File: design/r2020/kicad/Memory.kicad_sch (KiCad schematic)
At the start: 10 parts, among them U1 SST39SF040, U2 SST39SF040, U3 AS6C4008-55PCN, U4 AS6C4008-55PCN

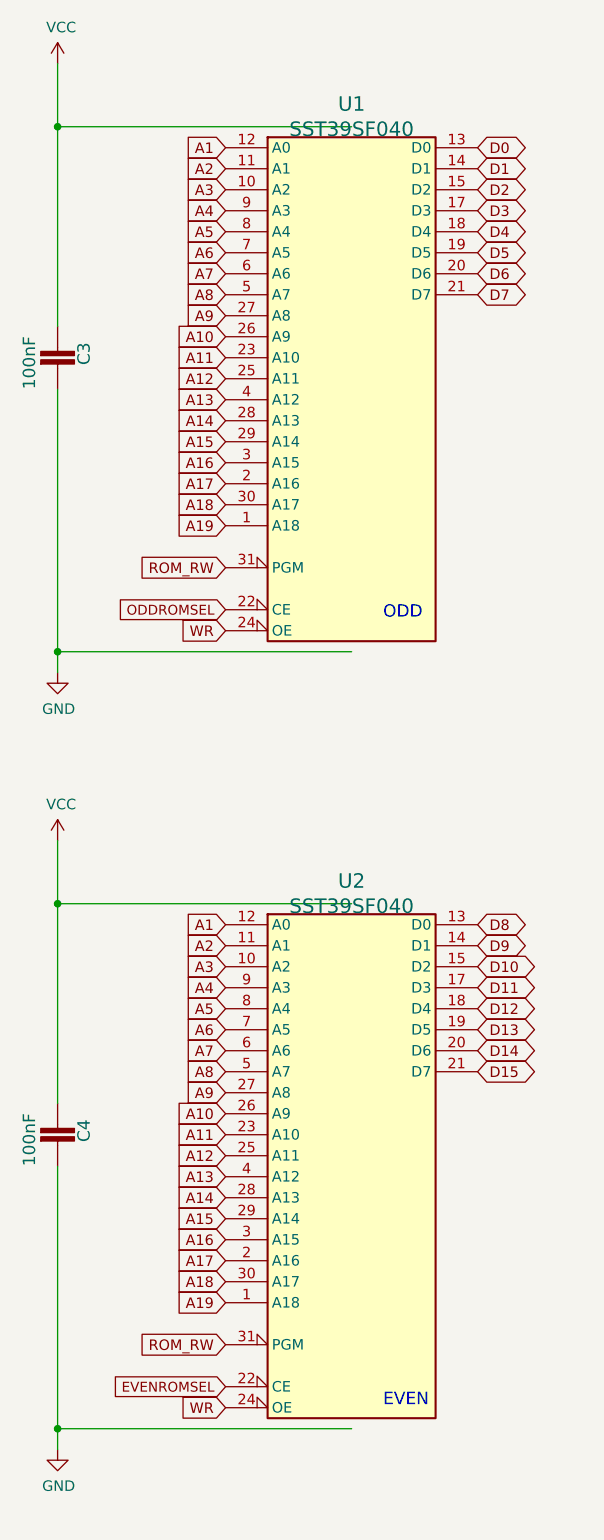
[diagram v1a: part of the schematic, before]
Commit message: Feature/kicad 7 (#388)
* Update r2 to Kicad 7
* Update r2020 to Kicad 7
* Complete Kicad 7 migration
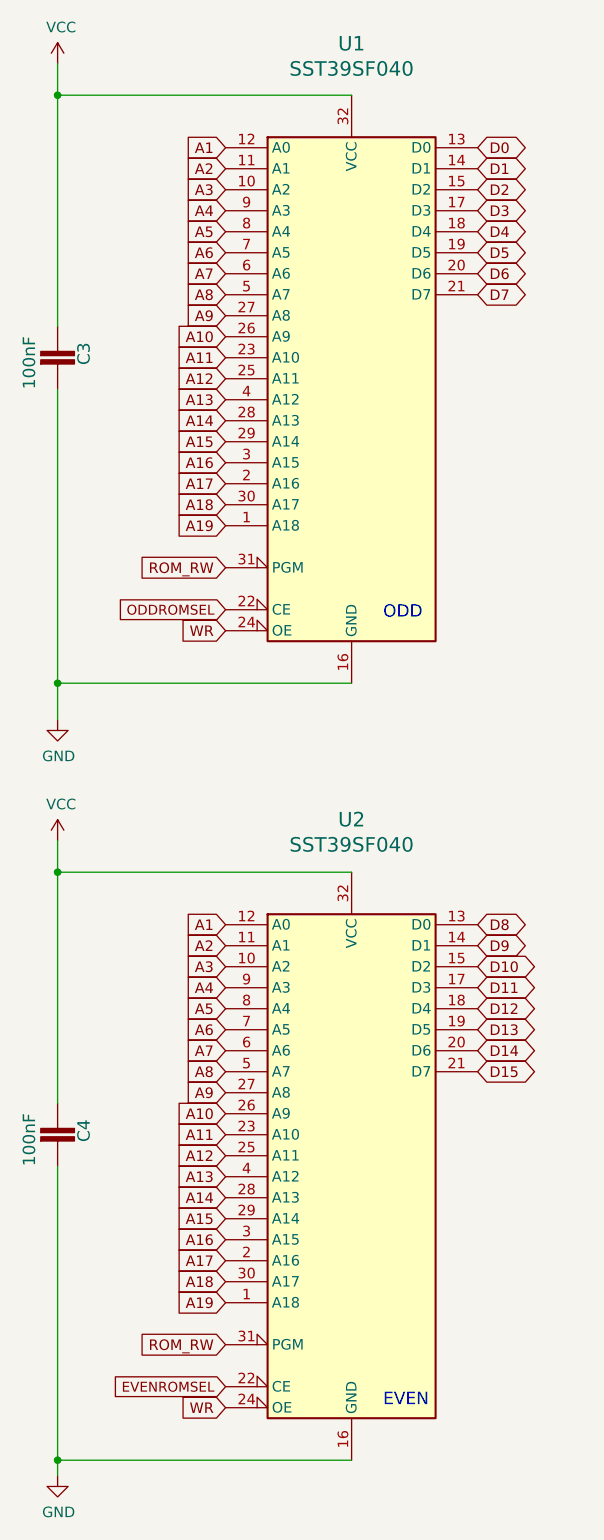
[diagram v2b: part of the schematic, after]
